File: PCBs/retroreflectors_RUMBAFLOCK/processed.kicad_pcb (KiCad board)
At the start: 2 copper layers, 6.3 x 6.4 mm, 7 parts, among them P1 INPUT, P2 ANTENNA

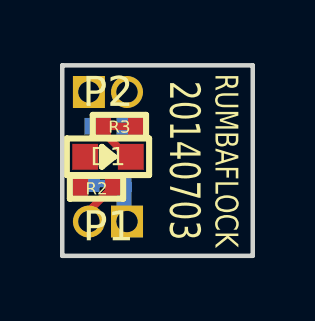
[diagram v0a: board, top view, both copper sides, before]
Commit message: recheck all circuits and clean up fill zone by rerouting the nets using freerouting and manually
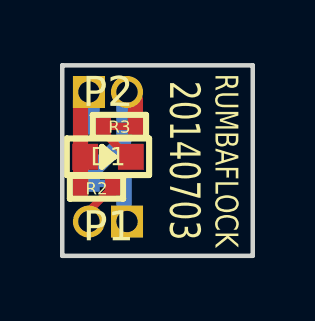
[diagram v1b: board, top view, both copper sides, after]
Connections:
- D1 pad 1: (no net) -> N-000005
- P2 pad 1: (no net) -> N-000005
- P2 pad 2: (no net) -> GND
- R1 pad 1: (no net) -> N-000005
- R1 pad 2: (no net) -> GND
- R2 pad 2: (no net) -> N-000005
- R3 pad 1: (no net) -> GND
- R4 pad 1: (no net) -> GND
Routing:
- net GND: track 0.00 -> 4.79 mm
- net N-000005: track 0.00 -> 4.60 mm
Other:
- board text added: "0703"
- board text removed: "703"

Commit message: clean psbc that are missed before
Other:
- board text added: "703"
- board text removed: "0703"
